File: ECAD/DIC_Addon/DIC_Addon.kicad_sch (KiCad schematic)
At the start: 115 parts, among them J1 WE 62702621621, Q1 FDN352AP, Q10 2N7002, Q11 FDN352AP, Q12 2N7002, Q13 FDN352AP, Q14 FDN352AP, Q15 2N7002, Q16 FDN352AP, Q17 FDN352AP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

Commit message: Finish Schematic for V3 PCB
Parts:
- removed D19, D20, D21, D22: Z 3.3V, Diode_SMD:D_SOD-323_HandSoldering, symbol Device:D
- removed Q19, Q20, Q21, Q22: 2N7002, Package_TO_SOT_SMD:SOT-23, symbol Transistor_FET:2N7002
- removed R43, R49, R54, R59: 100R 0603, Resistor_SMD:R_0603_1608Metric_Pad0.98x0.95mm_HandSolder, symbol Device:R
- removed R44, R51, R56, R61: 39kR 0603, Resistor_SMD:R_0603_1608Metric_Pad0.98x0.95mm_HandSolder, symbol Device:R
- removed R45, R48, R53, R58: 82kR 0603, Resistor_SMD:R_0603_1608Metric_Pad0.98x0.95mm_HandSolder, symbol Device:R
- removed R46, R52, R57, R62: 1kR 0603, Resistor_SMD:R_0603_1608Metric_Pad0.98x0.95mm_HandSolder, symbol Device:R
- removed R47, R50, R55, R60: 150kR 0603, Resistor_SMD:R_0603_1608Metric_Pad0.98x0.95mm_HandSolder, symbol Device:R
- TH1, TH2, TH3, TH4, TH5, TH6: value SMD1206B050TF/15 -> SMD1206B025TF
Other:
- note removed: "150k for 5V In. 150K || 39k -> 30,95k for 12V"
- moved on the sheet: GPIO1, GPIO2, J1

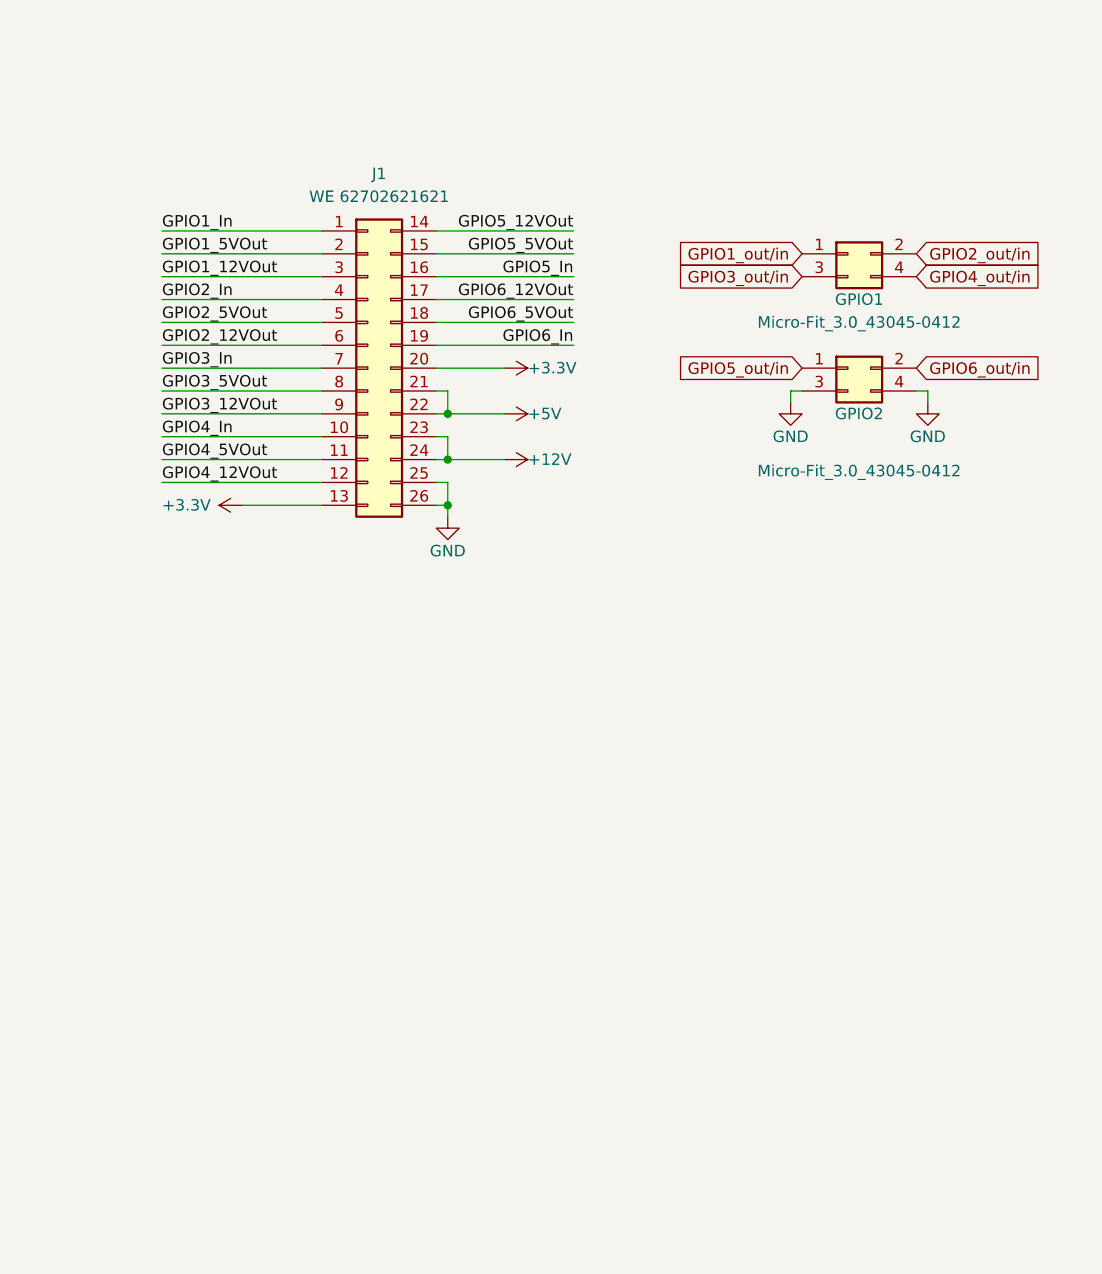
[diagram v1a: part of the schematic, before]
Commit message: switch to ribbon cable pcb interconnect
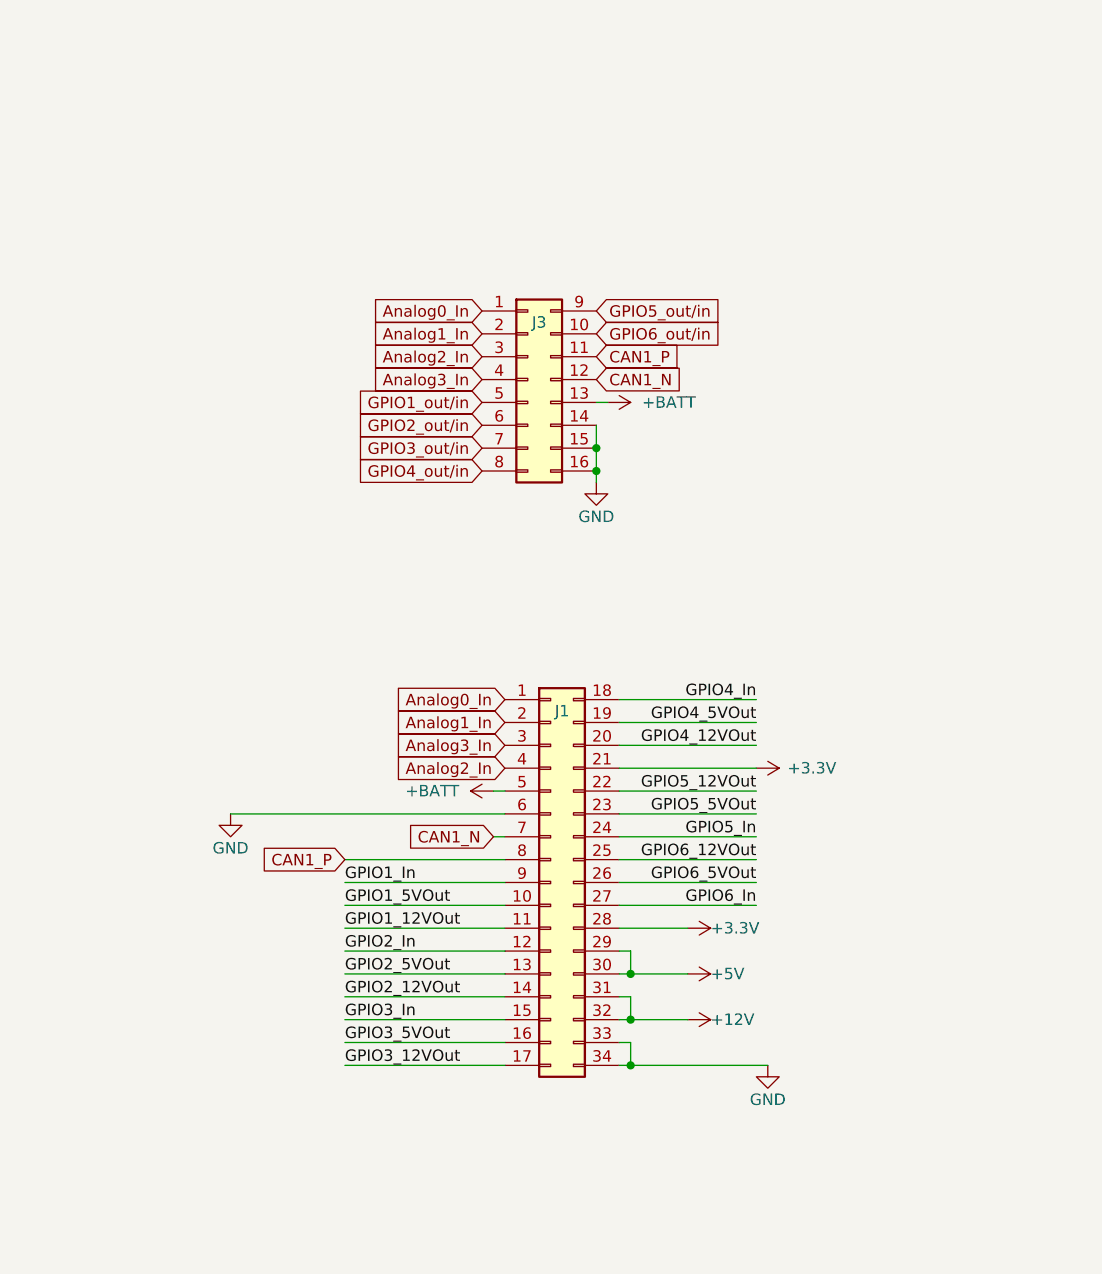
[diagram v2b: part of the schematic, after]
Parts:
- removed GPIO1, GPIO2: Micro-Fit_3.0_43045-0412, Lukas:Molex_Micro-Fit_3.0_43045-0412_2x02_P3.00mm_Vertical, symbol Lukas:Molex_Micro-Fit_3.0_43045-0412_2x02_P3.00mm_Vertical
- removed J1: WE 62702621621, Connector_PinHeader_1.27mm:PinHeader_2x13_P1.27mm_Vertical, symbol Connector_Generic:Conn_02x13_Top_Bottom
- added J1: WE 62702621621, Connector_PinHeader_1.27mm:PinHeader_2x17_P1.27mm_Vertical, symbol Connector_Generic:Conn_02x17_Top_Bottom
- added J3: WE 62702621621, Connector_PinHeader_1.27mm:PinHeader_2x07_P1.27mm_Vertical, symbol Connector_Generic:Conn_02x08_Top_Bottom
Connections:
- net +12V: now also J1.31 (Pin_31), J1.32 (Pin_32)
- net +3.3V: now also J1.21 (Pin_21), J1.28 (Pin_28)
- net +5V: now also J1.29 (Pin_29), J1.30 (Pin_30)
- net GND: now also J1.33 (Pin_33), J1.34 (Pin_34), J1.6 (Pin_6), J3.14 (Pin_14), J3.15 (Pin_15), J3.16 (Pin_16)
- net GPIO1_12VOut: now also J1.11 (Pin_11)
- net GPIO1_5VOut: now also J1.10 (Pin_10)
- net GPIO1_In: now also J1.9 (Pin_9)
- net GPIO1_out/in: now also J3.5 (Pin_5)
- net GPIO2_12VOut: now also J1.14 (Pin_14)
- net GPIO2_5VOut: now also J1.13 (Pin_13)
- net GPIO2_In: now also J1.12 (Pin_12)
- net GPIO2_out/in: now also J3.6 (Pin_6)
- net GPIO3_12VOut: now also J1.17 (Pin_17)
- net GPIO3_5VOut: now also J1.16 (Pin_16)
- net GPIO3_In: now also J1.15 (Pin_15)
- net GPIO3_out/in: now also J3.7 (Pin_7)
- net GPIO4_12VOut: now also J1.20 (Pin_20)
- net GPIO4_5VOut: now also J1.19 (Pin_19)
- net GPIO4_In: now also J1.18 (Pin_18)
- net GPIO4_out/in: now also J3.8 (Pin_8)
- net GPIO5_12VOut: now also J1.22 (Pin_22)
- net GPIO5_5VOut: now also J1.23 (Pin_23)
- net GPIO5_In: now also J1.24 (Pin_24)
- net GPIO5_out/in: now also J3.9 (Pin_9)
- net GPIO6_12VOut: now also J1.25 (Pin_25)
- net GPIO6_5VOut: now also J1.26 (Pin_26)
- net GPIO6_In: now also J1.27 (Pin_27)
- net GPIO6_out/in: now also J3.10 (Pin_10)
- new net +BATT: J1.5 (Pin_5), J3.13 (Pin_13)
- new net Analog0_In: J1.1 (Pin_1), J3.1 (Pin_1)
- new net Analog1_In: J1.2 (Pin_2), J3.2 (Pin_2)
- new net Analog2_In: J1.4 (Pin_4), J3.3 (Pin_3)
- new net Analog3_In: J1.3 (Pin_3), J3.4 (Pin_4)
- new net CAN1_N: J1.7 (Pin_7), J3.12 (Pin_12)
- new net CAN1_P: J1.8 (Pin_8), J3.11 (Pin_11)

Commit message: finisjed PCB projekt
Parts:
- removed J1: WE 62702621621, Connector_PinHeader_1.27mm:PinHeader_2x17_P1.27mm_Vertical, symbol Connector_Generic:Conn_02x17_Top_Bottom
- added J2, J4, J5, J6: Conn_02x05_Top_Bottom, Connector_PinSocket_1.27mm:PinSocket_2x05_P1.27mm_Vertical, symbol Connector_Generic:Conn_02x05_Top_Bottom
- J3: footprint Connector_PinHeader_1.27mm:PinHeader_2x07_P1.27mm_Vertical -> Connector_PinHeader_1.27mm:PinHeader_2x08_P1.27mm_Vertical
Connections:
- net +12V: now also J4.3 (Pin_3), J4.4 (Pin_4)
- net +3.3V: now also J4.7 (Pin_7), J4.8 (Pin_8)
- net +5V: now also J4.10 (Pin_10), J4.9 (Pin_9)
- net +BATT: now also J3.12 (Pin_12), J4.1 (Pin_1), J4.2 (Pin_2)
- net Analog0_In: now also J2.3 (Pin_3)
- net Analog1_In: now also J2.6 (Pin_6)
- net Analog2_In: now also J2.8 (Pin_8)
- net Analog3_In: now also J2.10 (Pin_10)
- net CAN1_N: now also J3.15 (Pin_15), J2.1 (Pin_1); no longer J3.12 (Pin_12)
- net CAN1_P: now also J3.14 (Pin_14), J2.2 (Pin_2); no longer J3.11 (Pin_11)
- net GND: now also J3.5 (Pin_5), J2.4 (Pin_4), J2.5 (Pin_5), J2.7 (Pin_7), J2.9 (Pin_9), J4.5 (Pin_5), J4.6 (Pin_6), J5.9 (Pin_9), J6.10 (Pin_10); no longer J3.14 (Pin_14), J3.15 (Pin_15)
- net GPIO1_12VOut: now also J5.10 (Pin_10)
- net GPIO1_5VOut: now also J5.8 (Pin_8)
- net GPIO1_In: now also J5.6 (Pin_6)
- net GPIO1_out/in: now also J3.6 (Pin_6); no longer J3.5 (Pin_5)
- net GPIO2_12VOut: now also J5.4 (Pin_4)
- net GPIO2_5VOut: now also J5.2 (Pin_2)
- net GPIO2_In: now also J5.1 (Pin_1)
- net GPIO2_out/in: now also J3.7 (Pin_7); no longer J3.6 (Pin_6)
- net GPIO3_12VOut: now also J5.3 (Pin_3)
- net GPIO3_5VOut: now also J5.5 (Pin_5)
- net GPIO3_In: now also J5.7 (Pin_7)
- net GPIO3_out/in: now also J3.8 (Pin_8); no longer J3.7 (Pin_7)
- net GPIO4_12VOut: now also J6.2 (Pin_2)
- net GPIO4_5VOut: now also J6.4 (Pin_4)
- net GPIO4_In: now also J6.8 (Pin_8)
- net GPIO4_out/in: now also J3.9 (Pin_9); no longer J3.8 (Pin_8)
- net GPIO5_12VOut: now also J6.6 (Pin_6)
- net GPIO5_5VOut: now also J6.1 (Pin_1)
- net GPIO5_In: now also J6.9 (Pin_9)
- net GPIO5_out/in: now also J3.10 (Pin_10); no longer J3.9 (Pin_9)
- net GPIO6_12VOut: now also J6.3 (Pin_3)
- net GPIO6_5VOut: now also J6.5 (Pin_5)
- net GPIO6_In: now also J6.7 (Pin_7)
- net GPIO6_out/in: now also J3.11 (Pin_11); no longer J3.10 (Pin_10)
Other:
- moved on the sheet: J3

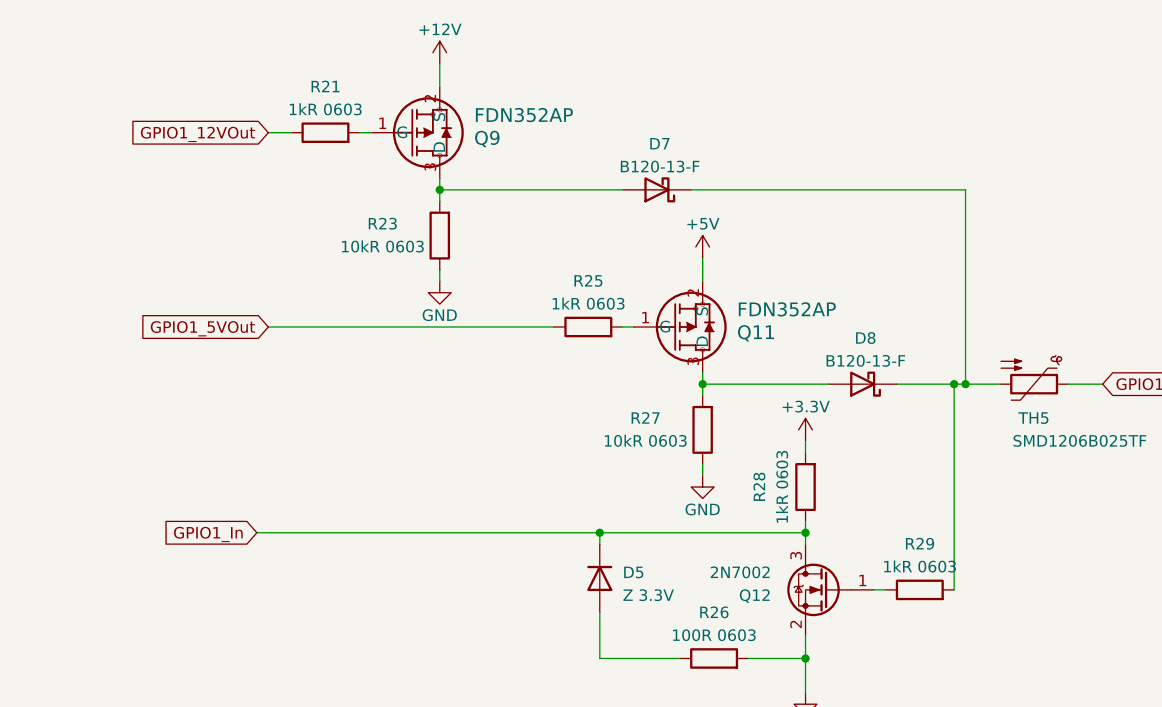
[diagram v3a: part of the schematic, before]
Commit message: bunch o SW
added all baseline code for Display LED, ADC etc.
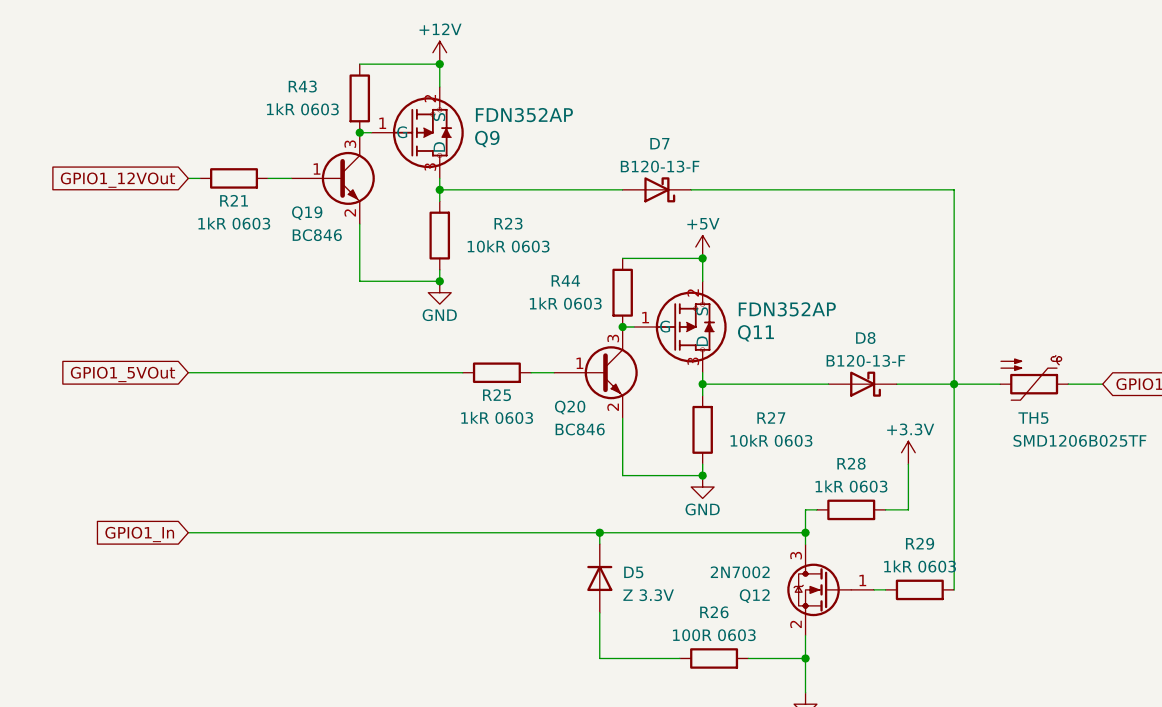
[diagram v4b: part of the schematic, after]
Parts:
- added Q19, Q20: BC846, Package_TO_SOT_SMD:SOT-23, symbol Transistor_BJT:BC846
- added R43, R44: 1kR 0603, Resistor_SMD:R_0603_1608Metric_Pad0.98x0.95mm_HandSolder, symbol Device:R
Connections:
- net +12V: now also R43.1
- net +5V: now also R44.1
- net GND: now also Q19.2 (E), Q20.2 (E)
- net at R25.2: now also Q20.1 (B); no longer Q11.1 (G)
- net at Q9.1 (G): now also Q19.3 (C), R43.2; no longer R21.2
- new net: Q11.1 (G), Q20.3 (C), R44.2
- new net: Q19.1 (B), R21.2
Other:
- moved on the sheet: R28
